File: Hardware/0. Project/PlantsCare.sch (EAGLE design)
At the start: 22 parts, among them CN1 ICSP, Q1 32.768 kHz, U1 MSP430FR4133

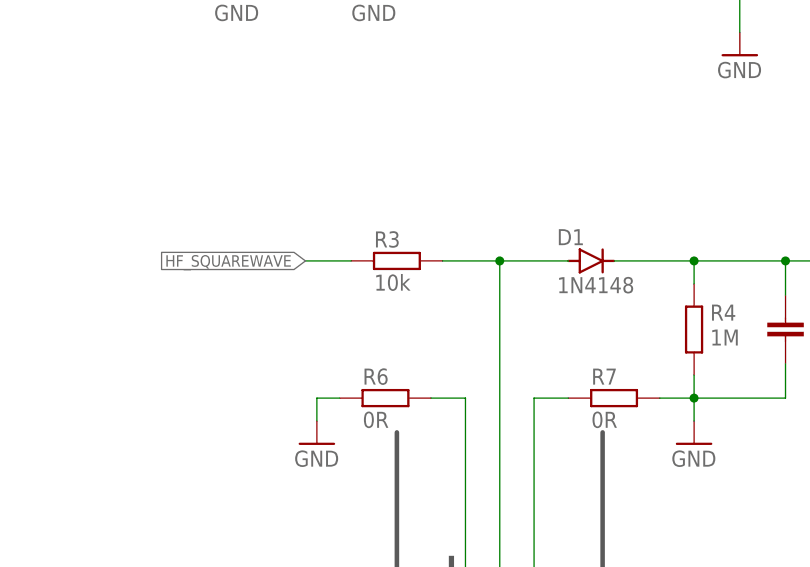
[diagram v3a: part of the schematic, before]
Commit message: R3 value changed to fix SENSOR_VOUT waveform
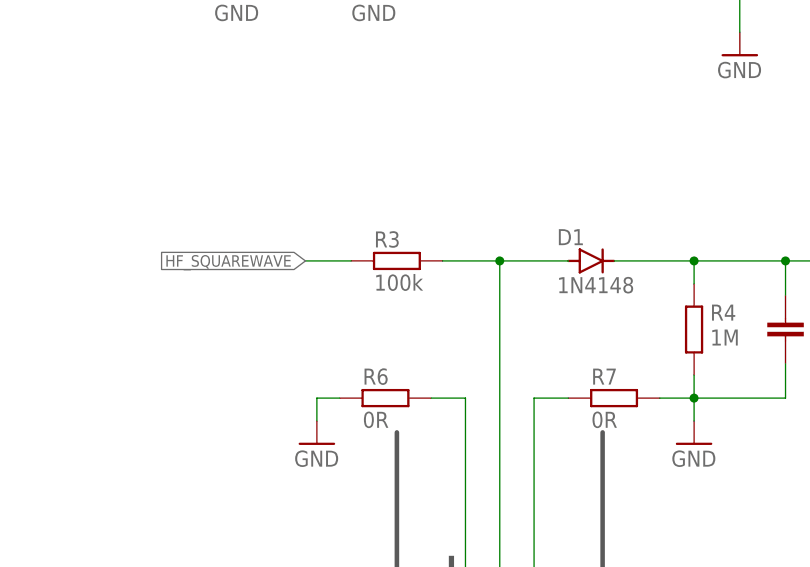
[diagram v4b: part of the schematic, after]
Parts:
- R3: value 10k -> 100k
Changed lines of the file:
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@@
 <setting verticaltext="up"/>
 </settings>
-<grid distance="0.05" unitdist="inch" unit="inch" style="lines" multiple="1" display="no" altdistance="0.01" altunitdist="inch" altunit="inch"/>
+<grid distance="0.1" unitdist="inch" unit="inch" style="lines" multiple="1" display="no" altdistance="0.01" altunitdist="inch" altunit="inch"/>
 <layers>
 <layer number="1" name="Top" color="4" fill="1" visible="no" active="no"/>
@@
 <part name="R4" library="rcl" library_urn="urn:adsk.eagle:library:334" deviceset="R-EU_" device="R0603" package3d_urn="urn:adsk.eagle:package:23555/3" value="1M"/>
 <part name="C7" library="rcl" library_urn="urn:adsk.eagle:library:334" deviceset="C-EU" device="C0603" package3d_urn="urn:adsk.eagle:package:23616/2" value="1 uF"/>
-<part name="R3" library="rcl" library_urn="urn:adsk.eagle:library:334" deviceset="R-EU_" device="R0603" package3d_urn="urn:adsk.eagle:package:23555/3" value="10k"/>
+<part name="R3" library="rcl" library_urn="urn:adsk.eagle:library:334" deviceset="R-EU_" device="R0603" package3d_urn="urn:adsk.eagle:package:23555/3" value="100k"/>
 <part name="PCB1" library="BLE-1010" deviceset="BLE-1010" device="" value="BLE-1010"/>
 <part name="GND5" library="supply1" library_urn="urn:adsk.eagle:library:371" deviceset="GND" device=""/>
